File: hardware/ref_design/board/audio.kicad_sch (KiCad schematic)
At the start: 17 parts, among them J4 53261-0271, Q3 2N7002, U7 FM8002A

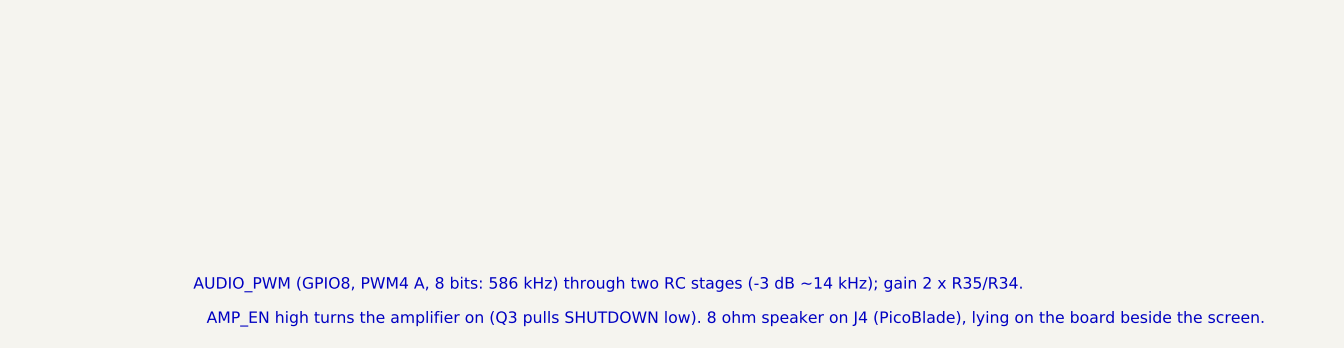
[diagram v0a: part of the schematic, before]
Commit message: ref_design levers: pins facing their nets, no REV straps, no UART, debug buttons and latch parts out of the strips
An experiment for Alex (not on ref-design-cellcut): make the board easier to route without
changing its size.
1. GPIOs: AUDIO_PWM 8 -> 31 (PWM7 B), AMP_EN 11 -> 34, BL_PWM 44 -> 28 (PWM6 A), PWR_HOLD
   2 -> 44, P2_START 34 -> 2, P2_SELECT 9 -> 4, SR_PL 28 -> 19 (datasheet Table 3 checked;
   U4's pin review updated)
2. REV0-REV3 and R48-R51 removed (the revision stays on the silkscreen)
3. J6 (UART) and C41 removed; SW18/SW19 out of the left strip into the left bezel below H4
   (U3 and its caps 2 mm down, JP1 below the core)
4. The latch's strip parts (Q1, R16, R15, C47, TP6, D8, Q7, R62, R63) up past the hole's
   top edge under seat 2's deck; C42 to the right bezel
tools/strip_load.py counts nets through each strip: 11/15 -> 8/11, parts 8/16 -> 3/5.
Routed clean on the first finished attempt (seed 3, 4.2 min); check_pcb and check_fit pass.

Co-Authored-By: Claude Opus 5.5 <noreply@anthropic.com>
Claude-Session: https://claude.ai/code/session_01Y3mFMxLYqNeyyedvbYuRwX
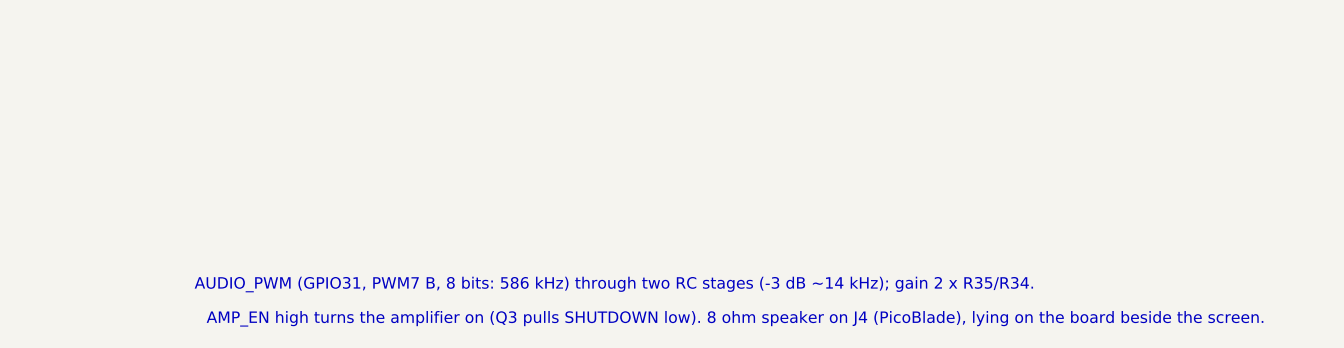
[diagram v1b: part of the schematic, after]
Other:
- note added: "AUDIO_PWM (GPIO31, PWM7 B, 8 bits: 586 kHz) through two RC stages (-3 dB ~14 kHz); gain 2 x R35/R34."
- note removed: "AUDIO_PWM (GPIO8, PWM4 A, 8 bits: 586 kHz) through two RC stages (-3 dB ~14 kHz); gain 2 x R35/R34."

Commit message: ref_design V&V round 3, schematic: R61 3.74k (DEC-31), R14 47k and R43 220k with no clamp (DEC-17), RN1-RN4 47k (DEC-24), U10 buffer on VBAT_SENSE, 10k B4460 NTC for TH1, J4 JST SH, pin reviews
Co-Authored-By: Claude Sonnet 5.5 <noreply@anthropic.com>
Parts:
- J4: value 53261-0271 -> SM02B-SRSS-TB; footprint Connector_Molex:Molex_PicoBlade_53261-0271_1x02-1MP_P1.25mm_Horizontal -> Connector_JST:JST_SH_SM02B-SRSS-TB_1x02-1MP_P1.00mm_Horizontal; LCSC C177225 -> C160402; MPN 532610271 -> SM02B-SRSS-TB(LF)(SN); Manufacturer Molex -> JST
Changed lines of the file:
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@@
 			)
 		)
-		(property "Value" "53261-0271"
+		(property "Value" "SM02B-SRSS-TB"
 			(at 177.8 76.2 0)
 			(show_name no)
@@
 			)
 		)
-		(property "Footprint" "Connector_Molex:Molex_PicoBlade_53261-0271_1x02-1MP_P1.25mm_Horizontal"
+		(property "Footprint" "Connector_JST:JST_SH_SM02B-SRSS-TB_1x02-1MP_P1.00mm_Horizontal"
 			(at 170.18 73.66 0)
 			(hide yes)
@@
 			)
 		)
-		(property "LCSC" "C177225"
+		(property "LCSC" "C160402"
 			(at 170.18 73.66 0)
 			(hide yes)
@@
 			)
 		)
-		(property "MPN" "532610271"
+		(property "MPN" "SM02B-SRSS-TB(LF)(SN)"
 			(at 170.18 73.66 0)
 			(hide yes)
@@
 			)
 		)
-		(property "Manufacturer" "Molex"
+		(property "Manufacturer" "JST"
 			(at 170.18 73.66 0)
 			(hide yes)
@@
 		(in_pos_files yes)
 		(dnp no)
-		(property "Reference" "#PWR093"
+		(property "Reference" "#PWR097"
 			(at 44.45 81.28 0)
 			(hide yes)
@@
 			(project "battler"
 				(path "/8922e0a8-6f76-52f6-b0ec-4de6a784796f/b41458f2-ed86-57fc-9560-c0eacbf9a6ae"
-					(reference "#PWR093")
+					(reference "#PWR097")
 					(unit 1)
 				)
@@
 		(in_pos_files yes)
 		(dnp no)
-		(property "Reference" "#PWR094"
+		(property "Reference" "#PWR098"
 			(at 67.31 81.28 0)
 			(hide yes)
@@
 			(project "battler"
 				(path "/8922e0a8-6f76-52f6-b0ec-4de6a784796f/b41458f2-ed86-57fc-9560-c0eacbf9a6ae"
-					(reference "#PWR094")
+					(reference "#PWR098")
 					(unit 1)
 				)
@@
 		(in_pos_files yes)
 		(dnp no)
-		(property "Reference" "#PWR095"
+		(property "Reference" "#PWR099"
 			(at 109.22 55.88 0)
 			(hide yes)
@@
 			(project "battler"
 				(path "/8922e0a8-6f76-52f6-b0ec-4de6a784796f/b41458f2-ed86-57fc-9560-c0eacbf9a6ae"
-					(reference "#PWR095")
+					(reference "#PWR099")
 					(unit 1)
 				)
@@
 		(in_pos_files yes)
 		(dnp no)
-		(property "Reference" "#PWR096"
+		(property "Reference" "#PWR100"
 			(at 132.08 63.5 0)
 			(hide yes)
@@
 			(project "battler"
 				(path "/8922e0a8-6f76-52f6-b0ec-4de6a784796f/b41458f2-ed86-57fc-9560-c0eacbf9a6ae"
-					(reference "#PWR096")
+					(reference "#PWR100")
 					(unit 1)
 				)
@@
 		(in_pos_files yes)
 		(dnp no)
-		(property "Reference" "#PWR097"
+		(property "Reference" "#PWR101"
 			(at 142.24 63.5 0)
 			(hide yes)
@@
 			(project "battler"
 				(path "/8922e0a8-6f76-52f6-b0ec-4de6a784796f/b41458f2-ed86-57fc-9560-c0eacbf9a6ae"
-					(reference "#PWR097")
+					(reference "#PWR101")
 					(unit 1)
 				)
@@
 		(in_pos_files yes)
 		(dnp no)
-		(property "Reference" "#PWR098"
+		(property "Reference" "#PWR102"
 			(at 127 88.9 0)
 			(hide yes)
@@
 			(project "battler"
 				(path "/8922e0a8-6f76-52f6-b0ec-4de6a784796f/b41458f2-ed86-57fc-9560-c0eacbf9a6ae"
-					(reference "#PWR098")
+					(reference "#PWR102")
 					(unit 1)
 				)
@@
 		(in_pos_files yes)
 		(dnp no)
-		(property "Reference" "#PWR099"
+		(property "Reference" "#PWR103"
 			(at 104.14 86.36 0)
 			(hide yes)
@@
 			(project "battler"
 				(path "/8922e0a8-6f76-52f6-b0ec-4de6a784796f/b41458f2-ed86-57fc-9560-c0eacbf9a6ae"
-					(reference "#PWR099")
+					(reference "#PWR103")
 					(unit 1)
 				)
@@
 		(in_pos_files yes)
 		(dnp no)
-		(property "Reference" "#PWR100"
+		(property "Reference" "#PWR104"
 			(at 99.06 106.68 0)
 			(hide yes)
@@
 			(project "battler"
 				(path "/8922e0a8-6f76-52f6-b0ec-4de6a784796f/b41458f2-ed86-57fc-9560-c0eacbf9a6ae"
-					(reference "#PWR100")
+					(reference "#PWR104")
 					(unit 1)
 				)
@@
 		(in_pos_files yes)
 		(dnp no)
-		(property "Reference" "#PWR101"
+		(property "Reference" "#PWR105"
 			(at 81.28 109.22 0)
 			(hide yes)
@@
 			(project "battler"
 				(path "/8922e0a8-6f76-52f6-b0ec-4de6a784796f/b41458f2-ed86-57fc-9560-c0eacbf9a6ae"
-					(reference "#PWR101")
-					(unit 1)
-				)
+					(reference "#PWR105")
+					(unit 1)
+				)

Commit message: ref_design ESP32-S3 schematic: WROOM-1U-N16R8 module, TLV75733P, 8-bit 8080 panel bus (R70-R78), microSD sheet, third 74HC165, BOOT/RESET and J7 pads, 1.5k audio filter; ERC 0, netlist and pin reviews pass
Footprints: battler:ESP32-S3-WROOM-1U (KiCad's without the 0.2 mm thermal vias, tools/fp_esp32.py) and the 4-pad J7. docs/esp32s3_pinmap_diff.md lists the differences from the proposal (no GPIO differs). Unverified: JLC Basic/Extended and stock of the new parts, the DM3AT card-detect pin order.

Co-Authored-By: Claude Sonnet 5.5 <noreply@anthropic.com>
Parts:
- added TP9: AUDIO_PWM, TestPoint:TestPoint_Pad_D1.0mm, symbol Connector:TestPoint
- R32, R33: value 1k -> 1.5k; LCSC C11702 -> C25867; MPN 0402WGF1001TCE -> 0402WGF1501TCE
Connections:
- net AUDIO_PWM: now also TP9.1
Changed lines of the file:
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@@
 	(title_block
 		(title "PWM audio and amplifier")
-		(rev "1")
+		(rev "2")
 		(company "Two-player handheld: reference design (REF-A)")
 		(comment 1 "Generated from board/design.py by tools/build_sch.py: edit design.py, not this sheet")
 	)
 	(junction
+		(at 31.75 73.66)
+		(diameter 0)
+		(color 0 0 0 0)
+	)
+	(junction
 		(at 44.45 73.66)
 		(diameter 0)
@@
 	(wire
 		(pts
-			(xy 27.94 73.66) (xy 33.02 73.66)
+			(xy 27.94 73.66) (xy 31.75 73.66)
+		)
+		(stroke
+			(width 0)
+			(type default)
+		)
+	)
+	(wire
+		(pts
+			(xy 31.75 73.66) (xy 33.02 73.66)
 		)
 		(stroke
@@
 			)
 		)
-		(property "Value" "1k"
+		(property "Value" "1.5k"
 			(at 36.83 76.276 90)
 			(show_name no)
@@
 			)
 		)
-		(property "LCSC" "C11702"
+		(property "LCSC" "C25867"
 			(at 36.83 73.66 0)
 			(hide yes)
@@
 			)
 		)
-		(property "MPN" "0402WGF1001TCE"
+		(property "MPN" "0402WGF1501TCE"
 			(at 36.83 73.66 0)
 			(hide yes)
@@
 			)
 		)
-		(property "Value" "1k"
+		(property "Value" "1.5k"
 			(at 55.88 76.276 90)
 			(show_name no)
@@
 			)
 		)
-		(property "LCSC" "C11702"
+		(property "LCSC" "C25867"
 			(at 55.88 73.66 0)
 			(hide yes)
@@
 			)
 		)
-		(property "MPN" "0402WGF1001TCE"
+		(property "MPN" "0402WGF1501TCE"
 			(at 55.88 73.66 0)
 			(hide yes)
@@
 	)
 	(symbol
+		(lib_id "Connector:TestPoint")
+		(at 31.75 73.66 0)
+		(unit 1)
+		(body_style 1)
+		(exclude_from_sim no)
+		(in_bom yes)
+		(on_board yes)
+		(in_pos_files yes)
+		(dnp no)
+		(property "Reference" "TP9"
+			(at 38.3122 69.55 0)
+			(show_name no)
+			(do_not_autoplace no)
+			(effects
+				(font
+					(size 1.27 1.27)
+				)
+			)
+		)
+		(property "Value" "AUDIO_PWM"
+			(at 38.3122 72.09 0)
+			(show_name no)
+			(do_not_autoplace no)
+			(effects
+				(font
+					(size 1.27 1.27)
+				)
+			)
+		)
+		(property "Footprint" "TestPoint:TestPoint_Pad_D1.0mm"
+			(at 31.75 73.66 0)
+			(hide yes)
+			(show_name no)
+			(do_not_autoplace no)
+			(effects
+				(font
+					(size 1.27 1.27)
+				)
+			)
+		)
+		(property "Datasheet" ""
+			(at 31.75 73.66 0)
+			(hide yes)
+			(show_name no)
+			(do_not_autoplace no)
+			(effects
+				(font
+					(size 1.27 1.27)
+				)
+			)
+		)
+		(property "Description" "test point"
+			(at 31.75 73.66 0)
+			(hide yes)
+			(show_name no)
+			(do_not_autoplace no)
+			(effects
+				(font
+					(size 1.27 1.27)
+				)
+			)
+		)
+		(property "BOM" "exclude"
+			(at 31.75 73.66 0)
+			(hide yes)
+			(show_name no)
+			(do_not_autoplace no)
+			(effects
+				(font
+					(size 1.27 1.27)
+				)
+			)
+		)
+		(pin "1"
+		)
+		(instances
+			(project "battler"
+				(path "/8922e0a8-6f76-52f6-b0ec-4de6a784796f/b41458f2-ed86-57fc-9560-c0eacbf9a6ae"
+					(reference "TP9")
+					(unit 1)
+				)
+			)
+		)
+	)
+	(symbol
 		(lib_id "Device:R")
 		(at 125.73 43.18 270)
@@
 		(in_pos_files yes)
 		(dnp no)
-		(property "Reference" "#PWR097"
+		(property "Reference" "#PWR105"
 			(at 44.45 81.28 0)
 			(hide yes)
@@
 			(project "battler"
 				(path "/8922e0a8-6f76-52f6-b0ec-4de6a784796f/b41458f2-ed86-57fc-9560-c0eacbf9a6ae"
-					(reference "#PWR097")
+					(reference "#PWR105")
 					(unit 1)
 				)
@@
 		(in_pos_files yes)
 		(dnp no)
-		(property "Reference" "#PWR098"
+		(property "Reference" "#PWR106"
 			(at 67.31 81.28 0)
 			(hide yes)
@@
 			(project "battler"
 				(path "/8922e0a8-6f76-52f6-b0ec-4de6a784796f/b41458f2-ed86-57fc-9560-c0eacbf9a6ae"
-					(reference "#PWR098")
+					(reference "#PWR106")
 					(unit 1)
 				)
@@
 		(in_pos_files yes)
 		(dnp no)
-		(property "Reference" "#PWR099"
+		(property "Reference" "#PWR107"
 			(at 109.22 55.88 0)
 			(hide yes)
@@
 			(project "battler"
 				(path "/8922e0a8-6f76-52f6-b0ec-4de6a784796f/b41458f2-ed86-57fc-9560-c0eacbf9a6ae"
-					(reference "#PWR099")
+					(reference "#PWR107")
 					(unit 1)
 				)
@@
 		(in_pos_files yes)
 		(dnp no)
-		(property "Reference" "#PWR100"
+		(property "Reference" "#PWR108"
 			(at 132.08 63.5 0)
 			(hide yes)
@@
 			(project "battler"
 				(path "/8922e0a8-6f76-52f6-b0ec-4de6a784796f/b41458f2-ed86-57fc-9560-c0eacbf9a6ae"
-					(reference "#PWR100")
+					(reference "#PWR108")
 					(unit 1)
 				)
@@
 		(in_pos_files yes)
 		(dnp no)
-		(property "Reference" "#PWR101"
+		(property "Reference" "#PWR109"
 			(at 142.24 63.5 0)
 			(hide yes)
@@
 			(project "battler"
 				(path "/8922e0a8-6f76-52f6-b0ec-4de6a784796f/b41458f2-ed86-57fc-9560-c0eacbf9a6ae"
-					(reference "#PWR101")
+					(reference "#PWR109")
 					(unit 1)
 				)
@@
 		(in_pos_files yes)
 		(dnp no)
-		(property "Reference" "#PWR102"
+		(property "Reference" "#PWR110"
 			(at 127 88.9 0)
 			(hide yes)
@@
 			(project "battler"
 				(path "/8922e0a8-6f76-52f6-b0ec-4de6a784796f/b41458f2-ed86-57fc-9560-c0eacbf9a6ae"
-					(reference "#PWR102")
+					(reference "#PWR110")
 					(unit 1)
 				)
@@
 		(in_pos_files yes)
 		(dnp no)
-		(property "Reference" "#PWR103"
+		(property "Reference" "#PWR111"
 			(at 104.14 86.36 0)
 			(hide yes)
@@
 			(project "battler"
 				(path "/8922e0a8-6f76-52f6-b0ec-4de6a784796f/b41458f2-ed86-57fc-9560-c0eacbf9a6ae"
-					(reference "#PWR103")
+					(reference "#PWR111")
 					(unit 1)
 				)
@@
 		(in_pos_files yes)
 		(dnp no)
-		(property "Reference" "#PWR104"
+		(property "Reference" "#PWR112"
 			(at 99.06 106.68 0)
 			(hide yes)
@@
 			(project "battler"
 				(path "/8922e0a8-6f76-52f6-b0ec-4de6a784796f/b41458f2-ed86-57fc-9560-c0eacbf9a6ae"
-					(reference "#PWR104")
+					(reference "#PWR112")
 					(unit 1)
 				)
@@
 		(in_pos_files yes)
 		(dnp no)
-		(property "Reference" "#PWR105"
+		(property "Reference" "#PWR113"
 			(at 81.28 109.22 0)
 			(hide yes)
@@
 			(project "battler"
 				(path "/8922e0a8-6f76-52f6-b0ec-4de6a784796f/b41458f2-ed86-57fc-9560-c0eacbf9a6ae"
-					(reference "#PWR105")
+					(reference "#PWR113")
 					(unit 1)
 				)
